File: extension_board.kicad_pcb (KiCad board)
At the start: 2 copper layers, 85.7 x 123.2 mm, 37 parts, among them CN1 Conn_02x20_Odd_Even, J1 Screw_Terminal_01x02, J2 Conn_01x02, J3 Conn_01x02, J4 Conn_01x02, J5 Conn_02x03_Odd_Even, J6 Conn_01x02, J7 Conn_02x14_Odd_Even, J8 Conn_02x10_Odd_Even, J9 Conn_02x19_Odd_Even, U1 LM334Z, U2 LM334Z, U3 LM334Z, U4 LM334Z

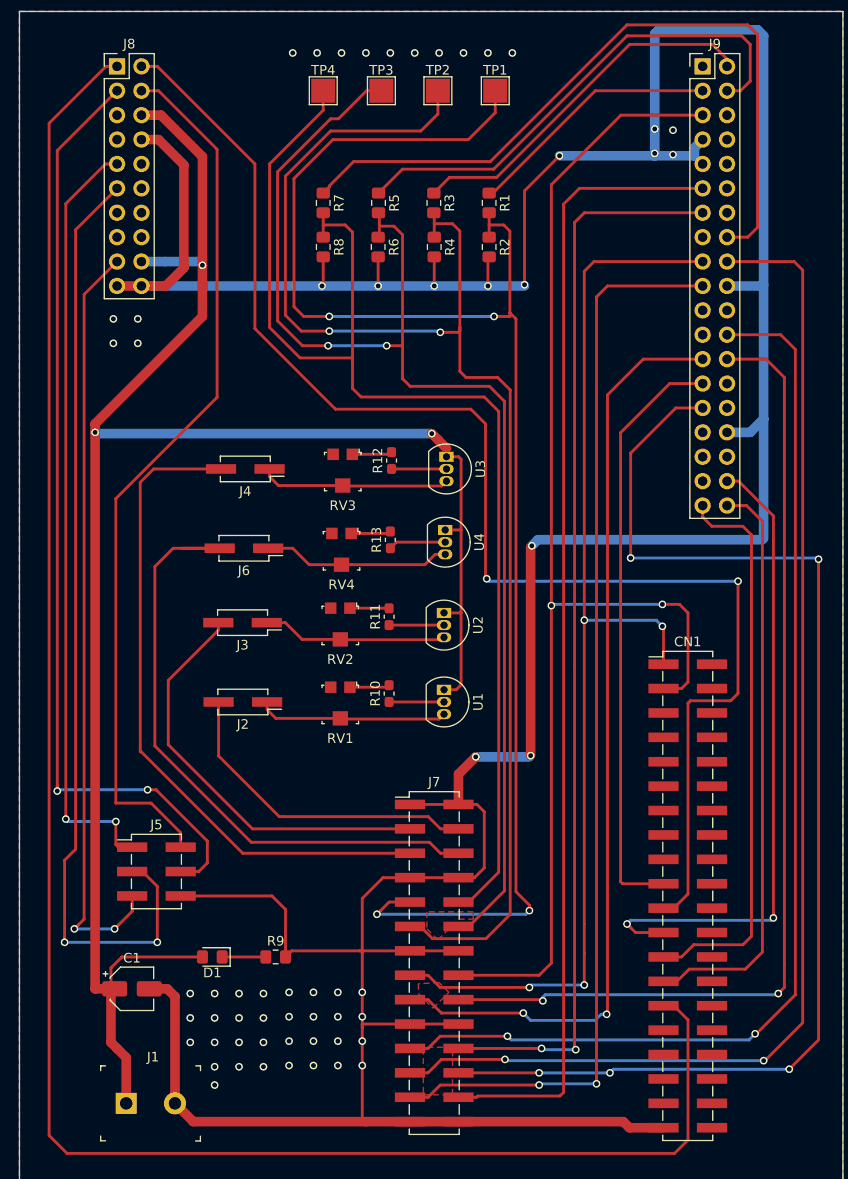
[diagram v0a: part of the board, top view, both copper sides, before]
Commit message: added labels on Top copper
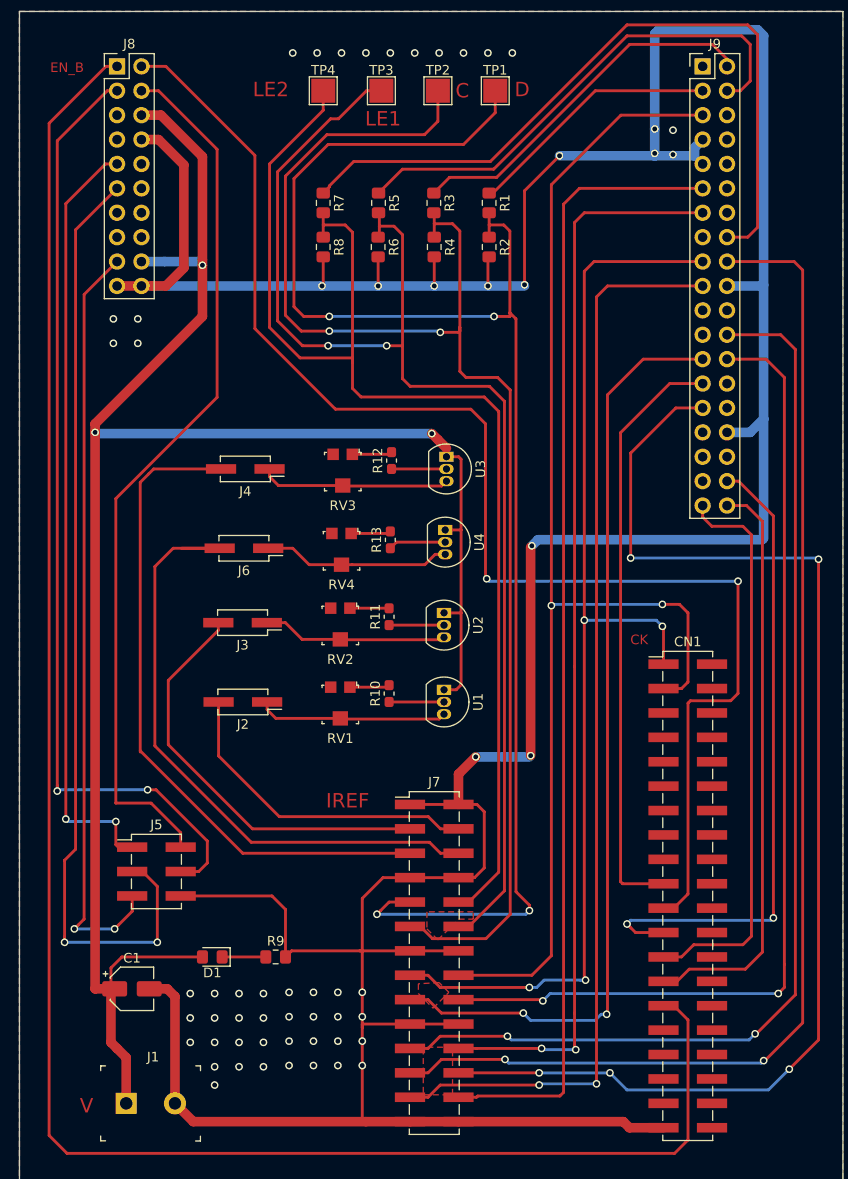
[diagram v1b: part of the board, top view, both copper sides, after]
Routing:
- net SPI_MOSI: track 128.9 -> 130.4 mm
- net PC12: track 98.8 -> 99.4 mm
- net EN_SUP2: track 144.1 -> 144.6 mm
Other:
- board text added: "C"
- board text added: "CK"
- board text added: "D"
- board text added: "EN_B"
- board text added: "IREF"
- board text added: "LE1"
- board text added: "LE2"
- board text added: "V"

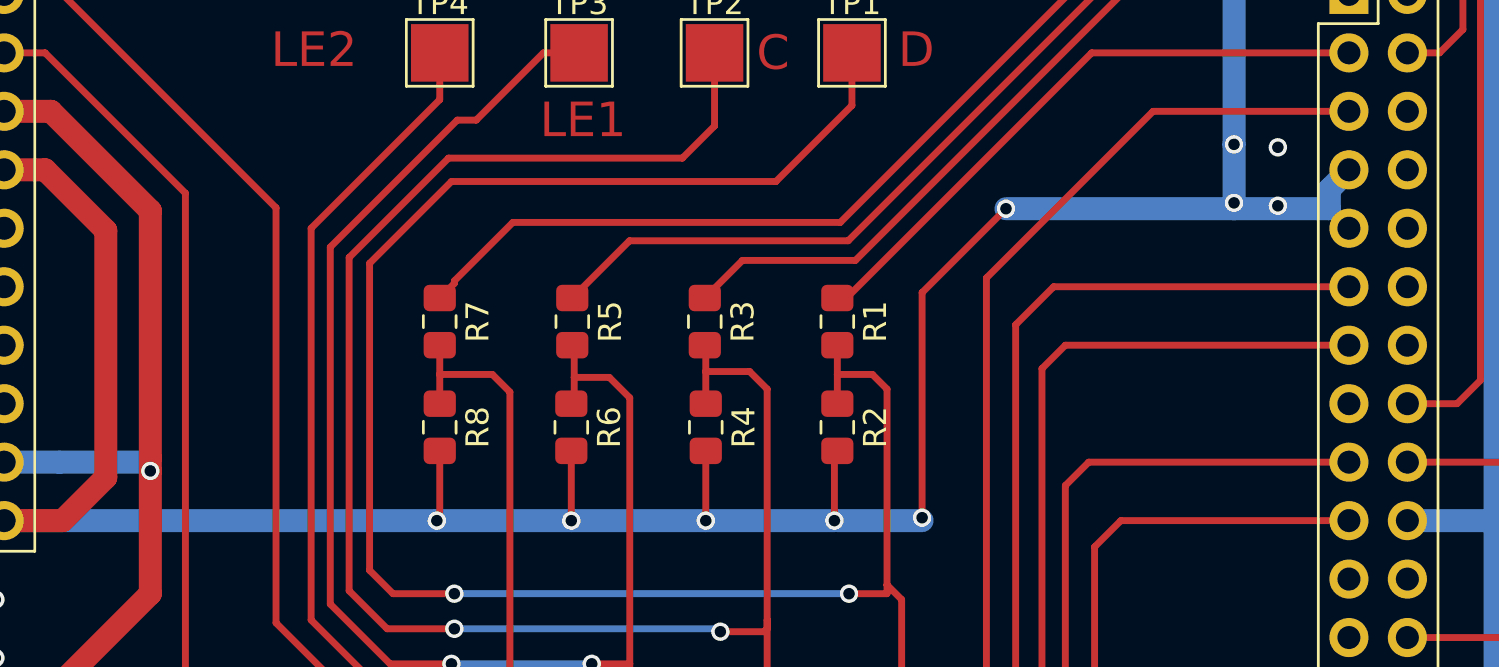
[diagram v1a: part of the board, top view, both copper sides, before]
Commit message: had shorted gnd and AVDD on the cn12 connector
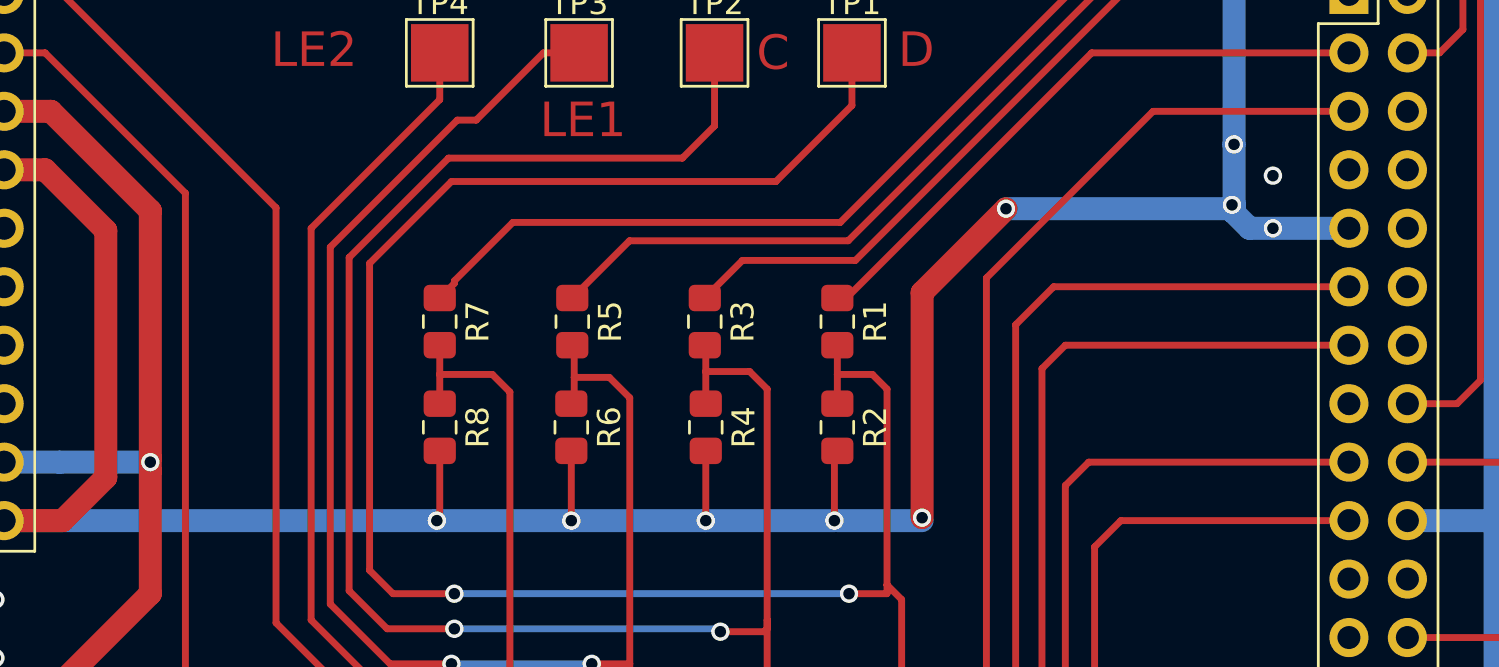
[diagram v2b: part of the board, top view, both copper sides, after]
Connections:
- J9 pad 7: GND -> Net-(J9-Pad7)
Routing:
- net GND: track 413.9 -> 412.2 mm
- net VDD: track 201.7 -> 201.2 mm
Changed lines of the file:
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@@
     (thickness 1.6)
     (drawings 13)
-    (tracks 623)
+    (tracks 620)
     (zones 0)
     (modules 37)
-    (nets 108)
+    (nets 109)
   )
   (page A4)
   (layers
     (0 F.Cu signal)
-    (31 B.Cu signal hide)
-    (32 B.Adhes user)
-    (33 F.Adhes user)
-    (34 B.Paste user)
-    (35 F.Paste user)
-    (36 B.SilkS user)
-    (37 F.SilkS user)
-    (38 B.Mask user)
-    (39 F.Mask user)
-    (40 Dwgs.User user)
-    (41 Cmts.User user)
-    (42 Eco1.User user)
-    (43 Eco2.User user)
-    (44 Edge.Cuts user)
-    (45 Margin user)
-    (46 B.CrtYd user)
-    (47 F.CrtYd user)
+    (31 B.Cu signal)
+    (32 B.Adhes user hide)
+    (33 F.Adhes user hide)
+    (34 B.Paste user hide)
+    (35 F.Paste user hide)
+    (36 B.SilkS user hide)
+    (37 F.SilkS user hide)
+    (38 B.Mask user hide)
+    (39 F.Mask user hide)
+    (40 Dwgs.User user hide)
+    (41 Cmts.User user hide)
+    (42 Eco1.User user hide)
+    (43 Eco2.User user hide)
+    (44 Edge.Cuts user hide)
+    (45 Margin user hide)
+    (46 B.CrtYd user hide)
+    (47 F.CrtYd user hide)
     (48 B.Fab user)
     (49 F.Fab user)
@@
     (solder_mask_min_width 0.25)
     (aux_axis_origin 0 0)
-    (visible_elements FEFFFF7F)
+    (visible_elements 7FFFFFFF)
     (pcbplotparams
       (layerselection 0x010fc_ffffffff)
@@
   (net 106 PA15)
   (net 107 PF7)
+  (net 108 "Net-(J9-Pad7)")
   (net_class Default "This is the default net class."
     (clearance 0.3)
@@
     (add_net "Net-(J9-Pad35)")
     (add_net "Net-(J9-Pad6)")
+    (add_net "Net-(J9-Pad7)")
     (add_net "Net-(J9-Pad8)")
     (add_net "Net-(R10-Pad1)")
@@
       (net 103 "Net-(J9-Pad8)"))
     (pad 7 thru_hole oval (at 0 7.62) (size 1.7 1.7) (drill 1) (layers *.Cu *.Mask)
-      (net 2 GND))
+      (net 108 "Net-(J9-Pad7)"))
     (pad 6 thru_hole oval (at 2.54 5.08) (size 1.7 1.7) (drill 1) (layers *.Cu *.Mask)
       (net 104 "Net-(J9-Pad6)"))
@@
   (segment (start -2.286 97.536) (end -2.286 105.029) (width 0.3) (layer F.Cu) (net 1))
   (segment (start -2.286 105.029) (end -2.794 105.537) (width 0.3) (layer F.Cu) (net 1))
-  (segment (start -33.147 60.96) (end -29.591 60.96) (width 1) (layer B.Cu) (net 1))
-  (segment (start -29.21 61.341) (end -29.21 61.341092) (width 0.3) (layer B.Cu) (net 1))
-  (segment (start -29.591 60.96) (end -29.21 61.341) (width 0.3) (layer B.Cu) (net 1))
-  (via (at -29.21 61.341092) (size 0.8) (drill 0.5) (layers F.Cu B.Cu) (net 1))
-  (segment (start -33.147 60.96) (end -35.56 60.96) (width 1) (layer B.Cu) (net 1))
   (segment (start -29.21 60.775407) (end -29.21 61.341092) (width 1) (layer F.Cu) (net 1))
   (segment (start -29.21 50.038) (end -29.21 60.775407) (width 1) (layer F.Cu) (net 1))
@@
   (segment (start -3.81 81.28) (end -3.81 80.391) (width 0.3) (layer F.Cu) (net 1))
   (segment (start -3.81 80.391) (end -4.699 79.502) (width 1) (layer F.Cu) (net 1))
+  (via (at -30.48 137.16) (size 0.8) (drill 0.5) (layers F.Cu B.Cu) (net 1))
+  (via (at -27.94 137.16) (size 0.8) (drill 0.5) (layers F.Cu B.Cu) (net 1))
+  (via (at -25.4 137.16) (size 0.8) (drill 0.5) (layers F.Cu B.Cu) (net 1))
+  (via (at -22.86 137.16) (size 0.8) (drill 0.5) (layers F.Cu B.Cu) (net 1))
+  (via (at -30.48 139.7) (size 0.8) (drill 0.5) (layers F.Cu B.Cu) (net 1))
+  (via (at -27.94 139.7) (size 0.8) (drill 0.5) (layers F.Cu B.Cu) (net 1))
+  (via (at -25.4 139.7) (size 0.8) (drill 0.5) (layers F.Cu B.Cu) (net 1))
+  (via (at -22.86 139.7) (size 0.8) (drill 0.5) (layers F.Cu B.Cu) (net 1))
+  (via (at -30.48 142.24) (size 0.8) (drill 0.5) (layers F.Cu B.Cu) (net 1))
+  (via (at -27.94 142.24) (size 0.8) (drill 0.5) (layers F.Cu B.Cu) (net 1))
+  (via (at -25.4 142.24) (size 0.8) (drill 0.5) (layers F.Cu B.Cu) (net 1))
+  (via (at -22.86 142.24) (size 0.8) (drill 0.5) (layers F.Cu B.Cu) (net 1))
+  (via (at -27.94 146.685) (size 0.8) (drill 0.5) (layers F.Cu B.Cu) (net 1))
+  (via (at -27.94 144.78) (size 0.8) (drill 0.5) (layers F.Cu B.Cu) (net 1))
+  (via (at -25.4 144.78) (size 0.8) (drill 0.5) (layers F.Cu B.Cu) (net 1))
+  (via (at -22.86 144.78) (size 0.8) (drill 0.5) (layers F.Cu B.Cu) (net 1))
+  (segment (start -33.147 60.96) (end -29.591 60.96) (width 1) (layer B.Cu) (net 1))
+  (segment (start -33.147 60.96) (end -35.56 60.96) (width 1) (layer B.Cu) (net 1))
+  (via (at -29.21 60.96) (size 0.8) (drill 0.5) (layers F.Cu B.Cu) (net 1))
   (segment (start -34.75 136.668) (end -32.877 136.668) (width 1) (layer F.Cu) (net 2))
   (segment (start -32.07 137.475) (end -32.07 148.59) (width 1) (layer F.Cu) (net 2))
@@
   (segment (start 0.508 60.597) (end 0.635 60.47) (width 0.3) (layer F.Cu) (net 2))
   (segment (start 0.508 63.5) (end 0.508 60.597) (width 0.3) (layer F.Cu) (net 2))
-  (segment (start 22.86 50.8) (end 22.010001 49.950001) (width 0.3) (layer B.Cu) (net 2))
   (via (at 7.961999 49.950001) (size 0.8) (drill 0.5) (layers F.Cu B.Cu) (net 2))
   (via (at 4.318 63.373) (size 0.8) (drill 0.5) (layers F.Cu B.Cu) (net 2))
-  (segment (start 7.961999 49.950001) (end 4.318 53.594) (width 0.3) (layer F.Cu) (net 2))
-  (segment (start 4.318 53.594) (end 4.318 63.373) (width 0.3) (layer F.Cu) (net 2))
+  (segment (start 7.961999 49.950001) (end 4.318 53.594) (width 1) (layer F.Cu) (net 2))
+  (segment (start 4.318 53.594) (end 4.318 63.373) (width 1) (layer F.Cu) (net 2))
   (segment (start 0.635 63.373) (end 0.508 63.5) (width 0.3) (layer B.Cu) (net 2))
   (segment (start 4.318 63.5) (end 0.635 63.5) (width 1) (layer B.Cu) (net 2))
@@
   (segment (start -21.971 127) (end -20.565 128.406) (width 0.3) (layer F.Cu) (net 2))
   (segment (start 17.867999 49.950001) (end 7.961999 49.950001) (width 1) (layer B.Cu) (net 2))
-  (segment (start 22.010001 49.950001) (end 17.867999 49.950001) (width 1) (layer B.Cu) (net 2))
   (segment (start 27.813 78.74) (end 25.4 78.74) (width 1) (layer B.Cu) (net 2))
   (segment (start 29.21 77.343) (end 27.813 78.74) (width 1) (layer B.Cu) (net 2))
@@
   (via (at -15.113 144.653) (size 0.8) (drill 0.5) (layers F.Cu B.Cu) (net 2))
   (via (at -12.573 144.653) (size 0.8) (drill 0.5) (layers F.Cu B.Cu) (net 2))
-  (via (at -30.48 137.16) (size 0.8) (drill 0.5) (layers F.Cu B.Cu) (net 1))
-  (via (at -27.94 137.16) (size 0.8) (drill 0.5) (layers F.Cu B.Cu) (net 1))
-  (via (at -25.4 137.16) (size 0.8) (drill 0.5) (layers F.Cu B.Cu) (net 1))
-  (via (at -22.86 137.16) (size 0.8) (drill 0.5) (layers F.Cu B.Cu) (net 1))
-  (via (at -30.48 139.7) (size 0.8) (drill 0.5) (layers F.Cu B.Cu) (net 1))
-  (via (at -27.94 139.7) (size 0.8) (drill 0.5) (layers F.Cu B.Cu) (net 1))
-  (via (at -25.4 139.7) (size 0.8) (drill 0.5) (layers F.Cu B.Cu) (net 1))
-  (via (at -22.86 139.7) (size 0.8) (drill 0.5) (layers F.Cu B.Cu) (net 1))
-  (via (at -30.48 142.24) (size 0.8) (drill 0.5) (layers F.Cu B.Cu) (net 1))
-  (via (at -27.94 142.24) (size 0.8) (drill 0.5) (layers F.Cu B.Cu) (net 1))
-  (via (at -25.4 142.24) (size 0.8) (drill 0.5) (layers F.Cu B.Cu) (net 1))
-  (via (at -22.86 142.24) (size 0.8) (drill 0.5) (layers F.Cu B.Cu) (net 1))
-  (via (at -27.94 146.685) (size 0.8) (drill 0.5) (layers F.Cu B.Cu) (net 1))
-  (via (at -27.94 144.78) (size 0.8) (drill 0.5) (layers F.Cu B.Cu) (net 1))
-  (via (at -25.4 144.78) (size 0.8) (drill 0.5) (layers F.Cu B.Cu) (net 1))
-  (via (at -22.86 144.78) (size 0.8) (drill 0.5) (layers F.Cu B.Cu) (net 1))
-  (segment (start 22.010001 49.109999) (end 22.86 48.26) (width 1) (layer B.Cu) (net 2))
-  (segment (start 22.010001 49.950001) (end 22.010001 49.109999) (width 1) (layer B.Cu) (net 2))
   (segment (start 17.867999 47.156001) (end 17.867999 37.250001) (width 1) (layer B.Cu) (net 2))
   (via (at 17.867999 47.156001) (size 0.8) (drill 0.5) (layers F.Cu B.Cu) (net 2))
-  (via (at 19.772999 47.283001) (size 0.8) (drill 0.5) (layers F.Cu B.Cu) (net 2))
-  (via (at 17.867999 49.696001) (size 0.8) (drill 0.5) (layers F.Cu B.Cu) (net 2))
-  (via (at 19.772999 49.823001) (size 0.8) (drill 0.5) (layers F.Cu B.Cu) (net 2))
+  (via (at 19.558 48.514) (size 0.8) (drill 0.5) (layers F.Cu B.Cu) (net 2))
+  (via (at 17.78 49.784) (size 0.8) (drill 0.5) (layers F.Cu B.Cu) (net 2))
+  (via (at 19.558 50.8) (size 0.8) (drill 0.5) (layers F.Cu B.Cu) (net 2))
+  (segment (start 18.542 50.8) (end 22.86 50.8) (width 1) (layer B.Cu) (net 2))
+  (segment (start 17.867999 49.696001) (end 17.867999 50.125999) (width 1) (layer B.Cu) (net 2))
+  (segment (start 17.867999 50.125999) (end 18.542 50.8) (width 1) (layer B.Cu) (net 2))
   (segment (start -7.605 135.255) (end -5.73 135.255) (width 0.3) (layer F.Cu) (net 3))
   (segment (start 11.557 60.96) (end 10.541 61.976) (width 0.3) (layer F.Cu) (net 3))
@@
   (segment (start -38.227 119.253) (end -43.18 119.253) (width 0.3) (layer B.Cu) (net 44))
   (segment (start -43.434 54.931919) (end -43.434 118.999) (width 0.3) (layer F.Cu) (net 44))
-  (segment (start -37.6 127) (end -36.525 127) (width 0.3) (layer F.Cu) (net 106))
   (via (at 13.208 145.415) (size 0.8) (drill 0.5) (layers F.Cu B.Cu) (net 45))
   (via (at 5.842 145.415) (size 0.8) (drill 0.5) (layers F.Cu B.Cu) (net 45))
@@
   (segment (start -9.017 90.17) (end -3.937 90.17) (width 0.3) (layer F.Cu) (net 77))
   (segment (start -9.652 90.805) (end -9.017 90.17) (width 0.3) (layer F.Cu) (net 77))
+  (segment (start -37.6 127) (end -36.525 127) (width 0.3) (layer F.Cu) (net 106))
   (segment (start -41.529 64.389) (end -41.529 129.413) (width 0.3) (layer F.Cu) (net 106))
   (via (at -42.545 130.429) (size 0.8) (drill 0.5) (layers F.Cu B.Cu) (net 106))

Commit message: gerber files and final files
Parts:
- removed CN1: Conn_02x20_Odd_Even, Connector_PinHeader_2.54mm:PinHeader_2x20_P2.54mm_Vertical_SMD
- added C2: 1u, Capacitor_SMD:C_0805_2012Metric_Pad1.15x1.40mm_HandSolder, F.Cu at (91.4, 59.7)
- added J10: Conn_01x09_Male, Connector_PinHeader_2.54mm:PinHeader_1x09_P2.54mm_Vertical_SMD_Pin1Left, F.Cu at (144.3, 123.4)
- added R14: 10K, Resistor_SMD:R_0805_2012Metric_Pad1.15x1.40mm_HandSolder, F.Cu at (90.4, 64.5)
- J2, J3, J4, J6: footprint Connector_PinHeader_2.54mm:PinHeader_2x01_P2.54mm_Vertical_SMD -> Connector_PinHeader_2.54mm:PinHeader_1x02_P2.54mm_Vertical
- TP1, TP2, TP3, TP4: footprint TestPoint:TestPoint_Pad_2.5x2.5mm -> TestPoint:TestPoint_Pad_1.0x1.0mm
- U1, U2, U3, U4: footprint Package_TO_SOT_THT:TO-92_Inline -> Package_TO_SOT_THT:TO-92_Inline_Wide
- moved J7 140.6 mm to (134.6, 118.4)
- moved J5 122.7 mm to (88.6, 123.3)
- moved U1 120.1 mm to (115.8, 113.3)
- moved J8 120.0 mm to (81.8, 46.7)
- moved R4 120.0 mm to (114.8, 65.5)
- moved R7 120.0 mm to (103.3, 61.0)
- moved R8 120.0 mm to (103.3, 65.5)
- moved TP1 120.0 mm to (121.2, 49.3)
- moved TP3 120.0 mm to (109.3, 49.3)
- moved TP4 120.0 mm to (103.3, 49.3)
- moved U2 120.0 mm to (115.8, 103.6)
- moved J9 120.0 mm to (142.7, 46.7)
- moved R1 120.0 mm to (120.5, 61.0)
- moved R2 120.0 mm to (120.5, 65.5)
- moved R3 120.0 mm to (114.8, 61.0)
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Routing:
- net GND: track 412.2 -> 261.0 mm, vias 43 -> 27
- net SPI_MOSI: track 130.4 -> 59.3 mm, vias 5 -> 0
- net EN_SUP2: track 144.6 -> 197.6 mm, vias 2 -> 0
- net SW2_VCTRL: track 105.1 -> 58.0 mm
- net SPI_NSS: track 130.0 -> 86.4 mm
- net 3v3_POW_EN: track 117.9 -> 78.5 mm
- net IC_DATA_1v: track 160.3 -> 121.1 mm
- net VDD: track 201.2 -> 238.0 mm, vias 19 -> 17
- net SW1_VCTRL: track 97.6 -> 61.3 mm, vias 2 -> 0
- net SYNTH_POW_EN: track 113.4 -> 81.2 mm, vias 2 -> 0
- net PF7: track 99.5 -> 71.8 mm
- net I2C_CLK: track 118.1 -> 91.8 mm
- net IC_CLK_1v: track 148.0 -> 121.8 mm, vias 2 -> 4
- net EN_SUP4: track 58.9 -> 84.7 mm, vias 0 -> 4
- net EN_SUP3: track 67.9 -> 42.4 mm, vias 2 -> 0
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- added copper zone on B.Cu, net GND
- added copper zone on F.Cu, net VDD
- removed copper zone on F.Cu, net GND
- removed copper zone on B.Cu, net VDD
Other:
- board size 85.7 x 123.2 mm -> 72.7 x 107.1 mm
- board text added: "Cm"
